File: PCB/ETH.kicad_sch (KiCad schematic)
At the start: 34 parts, among them J6 RJ45_Pulse_JXD6-0001NL, U6 DP83848C, Y2 50M

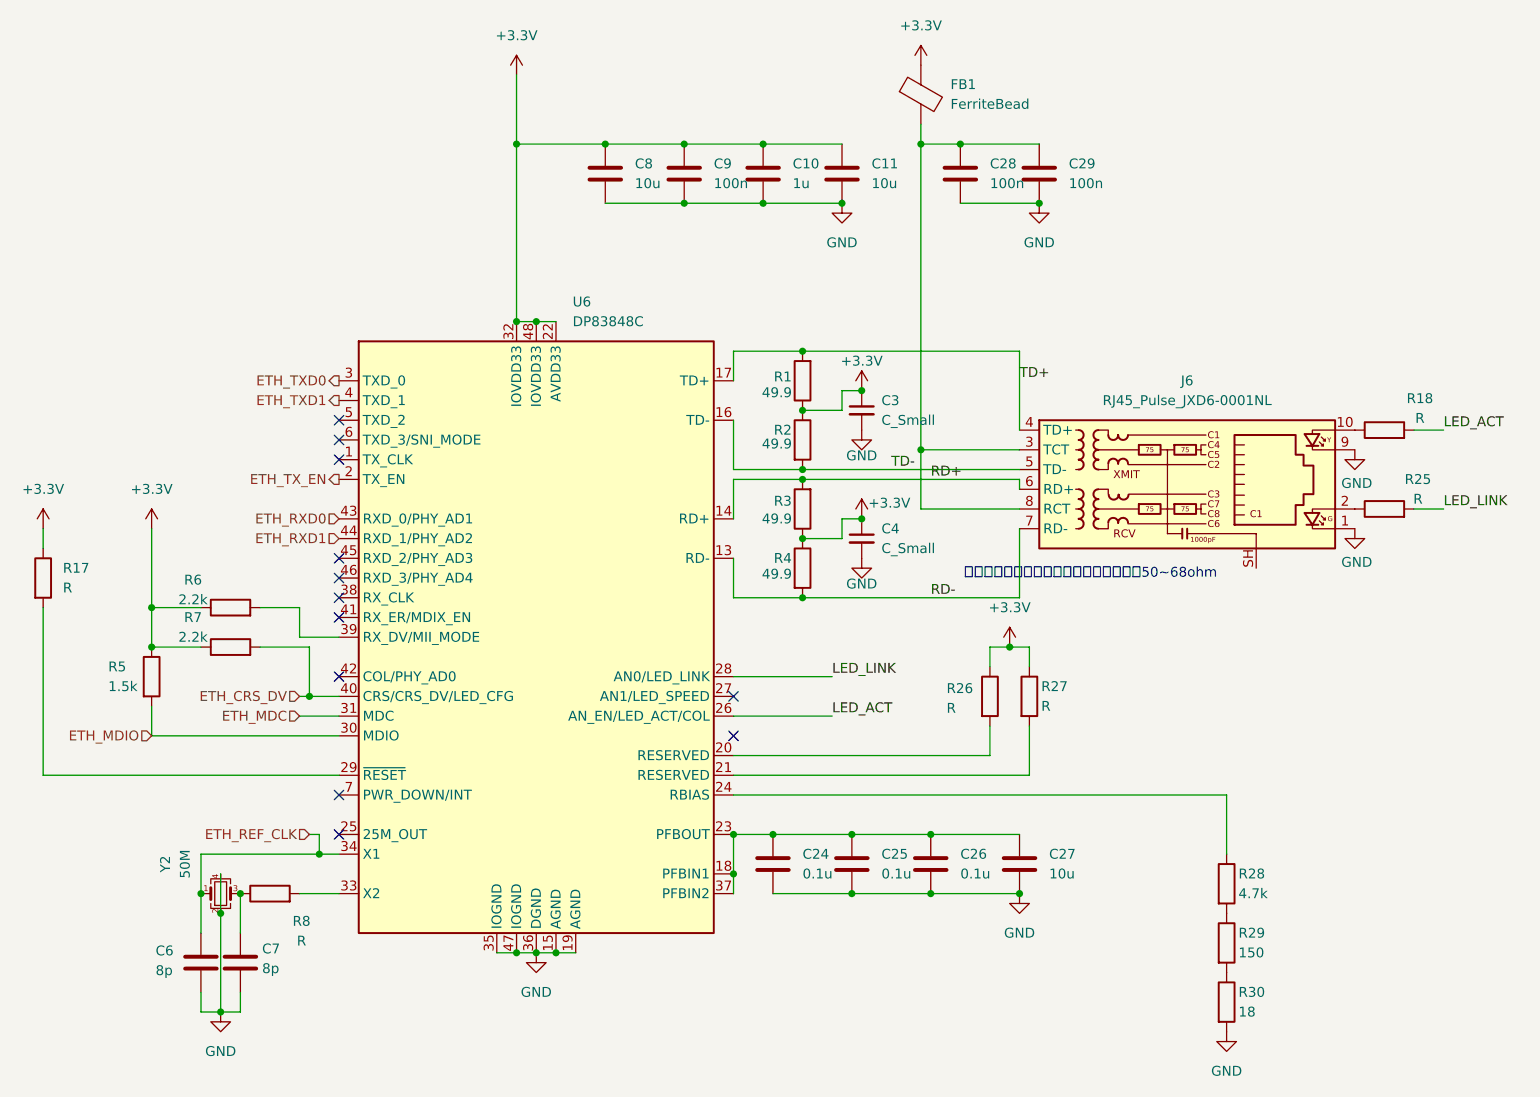
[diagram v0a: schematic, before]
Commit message: 電源以外配線おわり
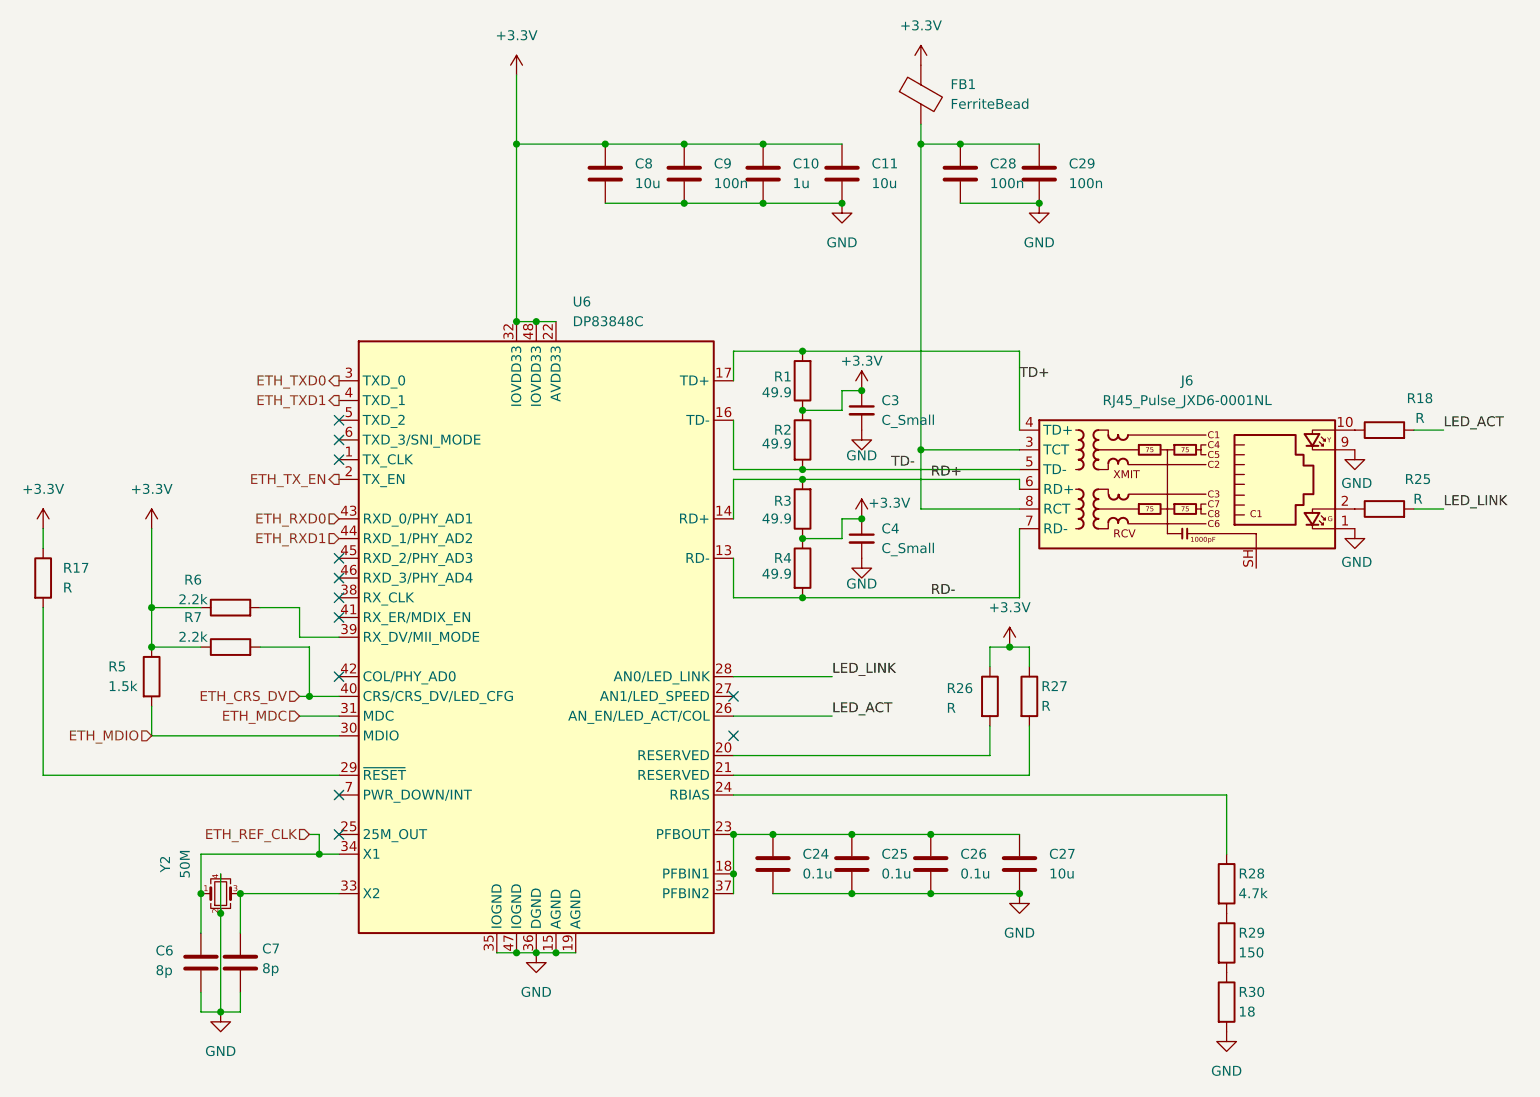
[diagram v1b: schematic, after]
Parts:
- removed R8: R, Resistor_SMD:R_0402_1005Metric_Pad0.72x0.64mm_HandSolder, symbol Device:R
- C10, C28, C29, C3, C4, C6, C7, C9: footprint Capacitor_SMD:C_0402_1005Metric_Pad0.74x0.62mm_HandSolder -> Capacitor_SMD:C_0603_1608Metric_Pad1.08x0.95mm_HandSolder
- R1, R17, R18, R2, R25, R26, R27, R28, R29, R3, R30, R4, R5, R6, R7: footprint Resistor_SMD:R_0402_1005Metric_Pad0.72x0.64mm_HandSolder -> Resistor_SMD:R_0603_1608Metric_Pad0.98x0.95mm_HandSolder
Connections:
- net at C7.1, Y2.3: now also U6.33 (X2)
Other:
- note removed: "差動ペア インピーダンスコントロール50~68ohm"
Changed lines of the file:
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@@
 	(generator_version "9.0")
 	(paper "A4")
-	(text "差動ペア　インピーダンスコントロール50~68ohm"
-		(exclude_from_sim no)
-		(at 211.074 97.282 0)
-		(effects
-			(font
-				(size 1.27 1.27)
-			)
-		)
-	)
 	(junction
 		(at 190.5 130.81)
@@
 	)
 	(junction
+		(at 101.6 138.43)
+		(diameter 0)
+		(color 0 0 0 0)
+	)
+	(junction
 		(at 99.06 153.67)
 		(diameter 0)
@@
 	)
 	(junction
-		(at 101.6 138.43)
-		(diameter 0)
-		(color 0 0 0 0)
-	)
-	(junction
 		(at 179.07 49.53)
 		(diameter 0)
@@
 	(wire
 		(pts
+			(xy 101.6 138.43) (xy 114.3 138.43)
+		)
+		(stroke
+			(width 0)
+			(type default)
+		)
+	)
+	(wire
+		(pts
 			(xy 179.07 92.71) (xy 179.07 90.17)
 		)
@@
 	(wire
 		(pts
-			(xy 109.22 138.43) (xy 114.3 138.43)
-		)
-		(stroke
-			(width 0)
-			(type default)
-		)
-	)
-	(wire
-		(pts
 			(xy 104.14 101.6) (xy 109.22 101.6)
 		)
@@
 			)
 		)
-		(property "Footprint" "Resistor_SMD:R_0402_1005Metric_Pad0.72x0.64mm_HandSolder"
+		(property "Footprint" "Resistor_SMD:R_0603_1608Metric_Pad0.98x0.95mm_HandSolder"
 			(at 196.342 113.03 90)
 			(effects
@@
 			)
 		)
-		(property "Footprint" "Resistor_SMD:R_0402_1005Metric_Pad0.72x0.64mm_HandSolder"
+		(property "Footprint" "Resistor_SMD:R_0603_1608Metric_Pad0.98x0.95mm_HandSolder"
 			(at 248.92 80.518 90)
 			(effects
@@
 			)
 		)
-		(property "Footprint" "Resistor_SMD:R_0402_1005Metric_Pad0.72x0.64mm_HandSolder"
+		(property "Footprint" "Resistor_SMD:R_0603_1608Metric_Pad0.98x0.95mm_HandSolder"
 			(at 226.822 137.16 90)
 			(effects
@@
 			)
 		)
-		(property "Footprint" "Resistor_SMD:R_0402_1005Metric_Pad0.72x0.64mm_HandSolder"
+		(property "Footprint" "Resistor_SMD:R_0603_1608Metric_Pad0.98x0.95mm_HandSolder"
 			(at 172.212 96.52 90)
 			(effects
@@
 			)
 		)
-		(property "Footprint" "Resistor_SMD:R_0402_1005Metric_Pad0.72x0.64mm_HandSolder"
+		(property "Footprint" "Resistor_SMD:R_0603_1608Metric_Pad0.98x0.95mm_HandSolder"
 			(at 100.33 108.458 90)
 			(effects
@@
 			)
 		)
-		(property "Footprint" "Resistor_SMD:R_0402_1005Metric_Pad0.72x0.64mm_HandSolder"
+		(property "Footprint" "Resistor_SMD:R_0603_1608Metric_Pad0.98x0.95mm_HandSolder"
 			(at 201.422 113.03 90)
 			(effects
@@
 			)
 		)
-		(property "Footprint" "Resistor_SMD:R_0402_1005Metric_Pad0.72x0.64mm_HandSolder"
+		(property "Footprint" "Resistor_SMD:R_0603_1608Metric_Pad0.98x0.95mm_HandSolder"
 			(at 88.392 110.49 90)
 			(effects
@@
 			)
 		)
-		(property "Footprint" "Resistor_SMD:R_0402_1005Metric_Pad0.72x0.64mm_HandSolder"
+		(property "Footprint" "Resistor_SMD:R_0603_1608Metric_Pad0.98x0.95mm_HandSolder"
 			(at 226.822 144.78 90)
 			(effects
@@
 			)
 		)
-		(property "Footprint" "Resistor_SMD:R_0402_1005Metric_Pad0.72x0.64mm_HandSolder"
+		(property "Footprint" "Resistor_SMD:R_0603_1608Metric_Pad0.98x0.95mm_HandSolder"
 			(at 74.422 97.79 90)
 			(effects
@@
 			)
 		)
-		(property "Footprint" "Resistor_SMD:R_0402_1005Metric_Pad0.72x0.64mm_HandSolder"
+		(property "Footprint" "Resistor_SMD:R_0603_1608Metric_Pad0.98x0.95mm_HandSolder"
 			(at 248.92 90.678 90)
 			(effects
@@
 			)
 		)
-		(property "Footprint" "Capacitor_SMD:C_0402_1005Metric_Pad0.74x0.62mm_HandSolder"
+		(property "Footprint" "Capacitor_SMD:C_0603_1608Metric_Pad1.08x0.95mm_HandSolder"
 			(at 102.5652 151.13 0)
 			(effects
@@
 			)
 		)
-		(property "Footprint" "Resistor_SMD:R_0402_1005Metric_Pad0.72x0.64mm_HandSolder"
+		(property "Footprint" "Resistor_SMD:R_0603_1608Metric_Pad0.98x0.95mm_HandSolder"
 			(at 100.33 103.378 90)
 			(effects
@@
 			)
 		)
-		(property "Footprint" "Resistor_SMD:R_0402_1005Metric_Pad0.72x0.64mm_HandSolder"
+		(property "Footprint" "Resistor_SMD:R_0603_1608Metric_Pad0.98x0.95mm_HandSolder"
 			(at 226.822 152.4 90)
 			(effects
@@
 			)
 		)
-		(property "Footprint" "Resistor_SMD:R_0402_1005Metric_Pad0.72x0.64mm_HandSolder"
+		(property "Footprint" "Resistor_SMD:R_0603_1608Metric_Pad0.98x0.95mm_HandSolder"
 			(at 172.212 80.01 90)
 			(effects
@@
 			)
 		)
-		(property "Footprint" "Capacitor_SMD:C_0402_1005Metric_Pad0.74x0.62mm_HandSolder"
+		(property "Footprint" "Capacitor_SMD:C_0603_1608Metric_Pad1.08x0.95mm_HandSolder"
 			(at 169.8752 49.53 0)
 			(effects
@@
 			)
 		)
-		(property "Footprint" "Resistor_SMD:R_0402_1005Metric_Pad0.72x0.64mm_HandSolder"
+		(property "Footprint" "Resistor_SMD:R_0603_1608Metric_Pad0.98x0.95mm_HandSolder"
 			(at 175.768 72.39 90)
 			(effects
@@
 			)
 		)
-		(property "Footprint" "Capacitor_SMD:C_0402_1005Metric_Pad0.74x0.62mm_HandSolder"
+		(property "Footprint" "Capacitor_SMD:C_0603_1608Metric_Pad1.08x0.95mm_HandSolder"
 			(at 205.4352 49.53 0)
 			(effects
@@
 			)
 		)
-		(property "Footprint" "Capacitor_SMD:C_0402_1005Metric_Pad0.74x0.62mm_HandSolder"
+		(property "Footprint" "Capacitor_SMD:C_0603_1608Metric_Pad1.08x0.95mm_HandSolder"
 			(at 195.2752 49.53 0)
 			(effects
@@
 			)
 		)
-		(property "Footprint" "Capacitor_SMD:C_0402_1005Metric_Pad0.74x0.62mm_HandSolder"
+		(property "Footprint" "Capacitor_SMD:C_0603_1608Metric_Pad1.08x0.95mm_HandSolder"
 			(at 181.61 76.2 0)
 			(effects
@@
 	)
 	(symbol
-		(lib_id "Device:R")
-		(at 105.41 138.43 90)
-		(unit 1)
-		(exclude_from_sim no)
-		(in_bom yes)
-		(on_board yes)
-		(dnp no)
-		(property "Reference" "R8"
-			(at 109.474 141.986 90)
-			(effects
-				(font
-					(size 1.27 1.27)
-				)
-			)
-		)
-		(property "Value" "R"
-			(at 109.474 144.526 90)
-			(effects
-				(font
-					(size 1.27 1.27)
-				)
-			)
-		)
-		(property "Footprint" "Resistor_SMD:R_0402_1005Metric_Pad0.72x0.64mm_HandSolder"
-			(at 105.41 140.208 90)
-			(effects
-				(font
-					(size 1.27 1.27)
-				)
-				(hide yes)
-			)
-		)
-		(property "Datasheet" "~"
-			(at 105.41 138.43 0)
-			(effects
-				(font
-					(size 1.27 1.27)
-				)
-				(hide yes)
-			)
-		)
-		(property "Description" "Resistor"
-			(at 105.41 138.43 0)
-			(effects
-				(font
-					(size 1.27 1.27)
-				)
-				(hide yes)
-			)
-		)
-		(pin "2"
-		)
-		(pin "1"
-		)
-		(instances
-			(project "kaniharu"
-				(path "/8cdd0db5-06ad-47be-921f-3bd5b446781a/45c69bb1-c038-44b2-b51a-d55622bb3f68"
-					(reference "R8")
-					(unit 1)
-				)
-			)
-		)
-	)
-	(symbol
 		(lib_id "power:GND")
 		(at 245.11 81.28 0)
@@
 			)
 		)
-		(property "Footprint" "Capacitor_SMD:C_0402_1005Metric_Pad0.74x0.62mm_HandSolder"
+		(property "Footprint" "Capacitor_SMD:C_0603_1608Metric_Pad1.08x0.95mm_HandSolder"
 			(at 181.61 92.71 0)
 			(effects
@@
 			)
 		)
-		(property "Footprint" "Capacitor_SMD:C_0402_1005Metric_Pad0.74x0.62mm_HandSolder"
+		(property "Footprint" "Capacitor_SMD:C_0603_1608Metric_Pad1.08x0.95mm_HandSolder"
 			(at 97.4852 151.13 0)
 			(effects
@@
 			)
 		)
-		(property "Footprint" "Resistor_SMD:R_0402_1005Metric_Pad0.72x0.64mm_HandSolder"
+		(property "Footprint" "Resistor_SMD:R_0603_1608Metric_Pad0.98x0.95mm_HandSolder"
 			(at 175.768 88.9 90)
 			(effects
@@
 			)
 		)
-		(property "Footprint" "Capacitor_SMD:C_0402_1005Metric_Pad0.74x0.62mm_HandSolder"
+		(property "Footprint" "Capacitor_SMD:C_0603_1608Metric_Pad1.08x0.95mm_HandSolder"
 			(at 159.7152 49.53 0)
 			(effects

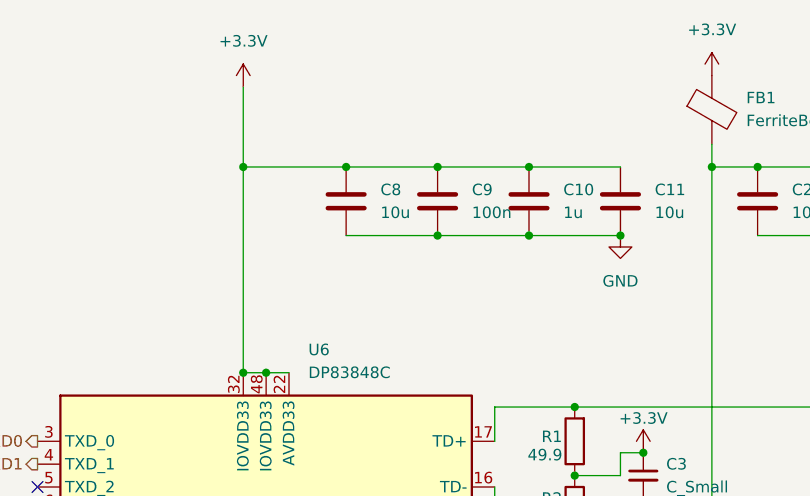
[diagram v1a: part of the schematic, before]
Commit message: update
電源配線した
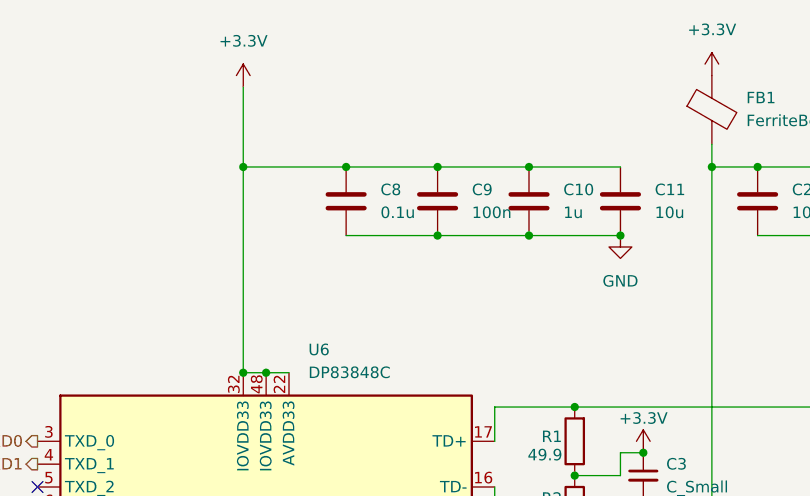
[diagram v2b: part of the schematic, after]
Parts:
- C8: value 10u -> 0.1u
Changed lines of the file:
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@@
 			)
 		)
-		(property "Value" "10u"
+		(property "Value" "0.1u"
 			(at 152.4 46.9899 0)
 			(effects
